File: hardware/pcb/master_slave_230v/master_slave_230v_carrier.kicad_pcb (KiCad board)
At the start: 2 copper layers, 126 x 66 mm, 24 parts, among them J1 AC_IN, J2 5V_SERVICE, J3A MASTER_L, J3B MASTER_R, J4A SLAVE_L, J4B SLAVE_R, J5 PHASE_OUT, J6 MASTER_SIG, J7 SLAVE_SIG, J8 MASTER_DEVKIT_BRIDGE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

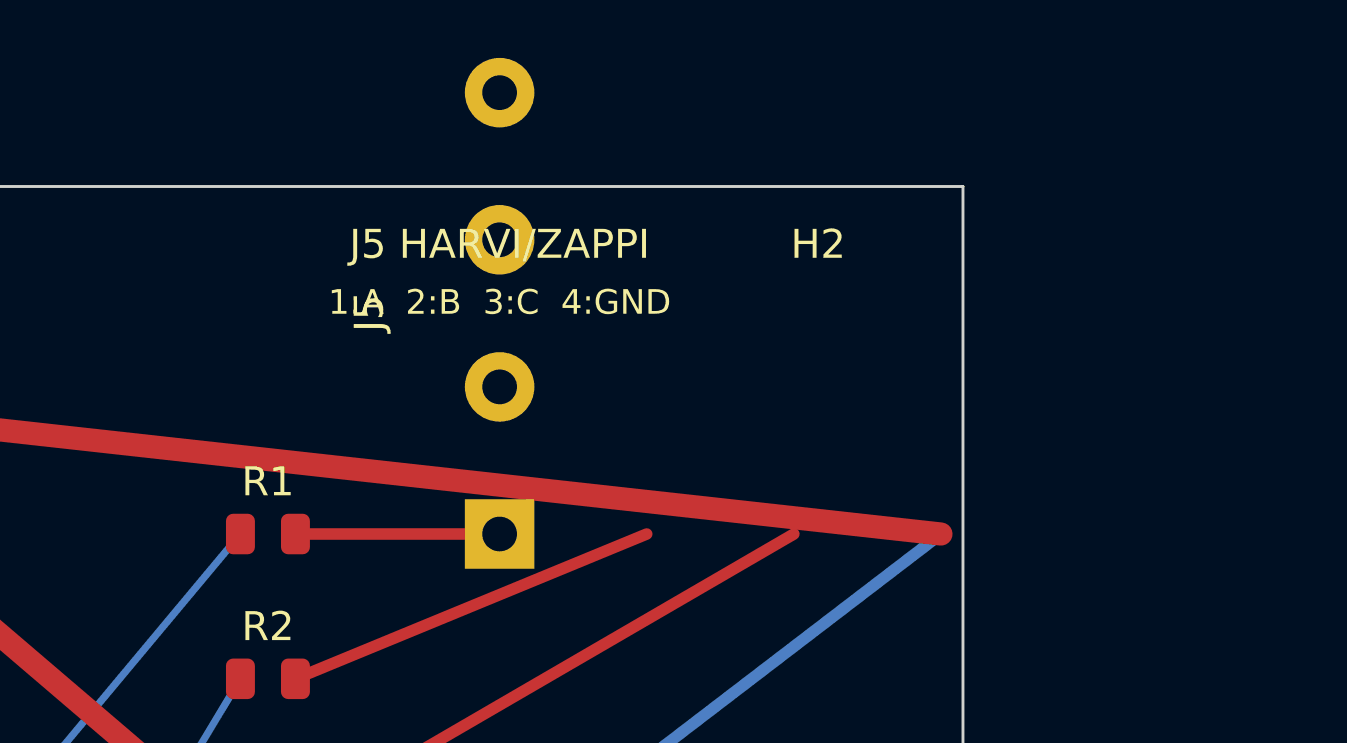
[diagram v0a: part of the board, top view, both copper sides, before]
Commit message: add display
show values/graph
fallback single mode
 -> Phase A = Sum
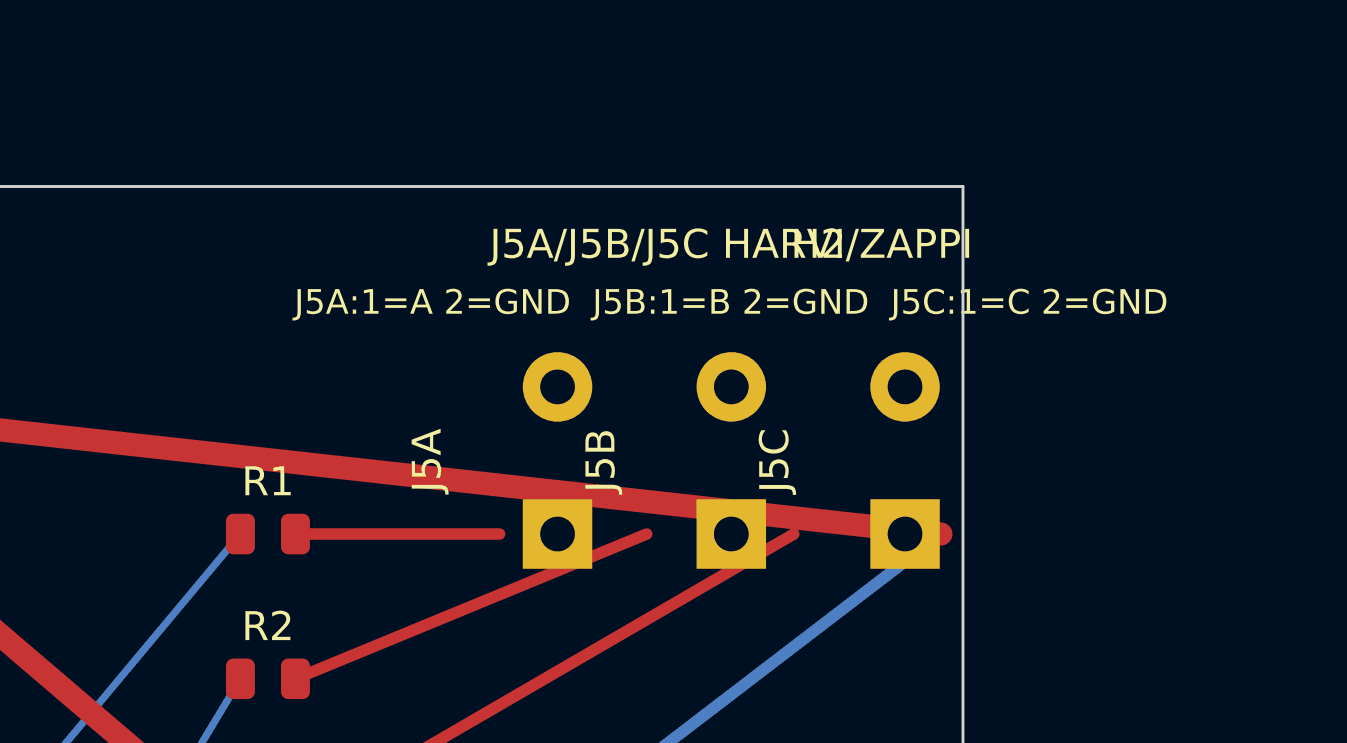
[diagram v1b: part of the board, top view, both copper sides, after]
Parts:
- removed J5: PHASE_OUT, TerminalBlock_Phoenix:TerminalBlock_Phoenix_MKDS-1,5-4_5.08mm
- added J5A: PHASE_A_OUT, TerminalBlock_Phoenix:TerminalBlock_Phoenix_MKDS-1,5-2_5.08mm, F.Cu at (112.0, 12.0)
- added J5B: PHASE_B_OUT, TerminalBlock_Phoenix:TerminalBlock_Phoenix_MKDS-1,5-2_5.08mm, F.Cu at (118.0, 12.0)
- added J5C: PHASE_C_OUT, TerminalBlock_Phoenix:TerminalBlock_Phoenix_MKDS-1,5-2_5.08mm, F.Cu at (124.0, 12.0)
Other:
- board text added: "J5A/J5B/J5C HARVI/ZAPPI"
- board text added: "J5A:1=A 2=GND J5B:1=B 2=GND J5C:1=C 2=GND"
- board text removed: "1:A 2:B 3:C 4:GND"
- board text removed: "J5 HARVI/ZAPPI"
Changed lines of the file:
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@@
   (gr_text "1:+5V  2:GND" (at 84 4 0) (layer "F.SilkS")
     (effects (font (size 0.85 0.85) (thickness 0.12))))
-  (gr_text "J5 HARVI/ZAPPI" (at 110 2 0) (layer "F.SilkS")
+  (gr_text "J5A/J5B/J5C HARVI/ZAPPI" (at 118 2 0) (layer "F.SilkS")
     (effects (font (size 1 1) (thickness 0.15))))
-  (gr_text "1:A  2:B  3:C  4:GND" (at 110 4 0) (layer "F.SilkS")
+  (gr_text "J5A:1=A 2=GND  J5B:1=B 2=GND  J5C:1=C 2=GND" (at 118 4 0) (layer "F.SilkS")
     (effects (font (size 0.85 0.85) (thickness 0.12))))
   (gr_text "HV ZONE" (at 22 33 90) (layer "F.SilkS")
@@
     (pad "2" thru_hole circle (at 5.08 0 90) (size 2.4 2.4) (drill 1.2) (layers "*.Cu" "*.Mask") (net 7 "GND_ISO"))
   )
-  (footprint "TerminalBlock_Phoenix:TerminalBlock_Phoenix_MKDS-1,5-4_5.08mm" (layer "F.Cu")
-    (at 110 12 90)
-    (property "Reference" "J5" (at 7.62 -4.5 90) (layer "F.SilkS")
+  (footprint "TerminalBlock_Phoenix:TerminalBlock_Phoenix_MKDS-1,5-2_5.08mm" (layer "F.Cu")
+    (at 112 12 90)
+    (property "Reference" "J5A" (at 2.54 -4.5 90) (layer "F.SilkS")
       (effects (font (size 1 1) (thickness 0.15))))
-    (property "Value" "PHASE_OUT" (at 7.62 4.5 90) (layer "F.Fab")
+    (property "Value" "PHASE_A_OUT" (at 2.54 4.5 90) (layer "F.Fab")
       (effects (font (size 1 1) (thickness 0.15))))
     (pad "1" thru_hole rect (at 0 0 90) (size 2.4 2.4) (drill 1.2) (layers "*.Cu" "*.Mask") (net 10 "PHASE_A_OUT"))
-    (pad "2" thru_hole circle (at 5.08 0 90) (size 2.4 2.4) (drill 1.2) (layers "*.Cu" "*.Mask") (net 11 "PHASE_B_OUT"))
-    (pad "3" thru_hole circle (at 10.16 0 90) (size 2.4 2.4) (drill 1.2) (layers "*.Cu" "*.Mask") (net 12 "PHASE_C_OUT"))
-    (pad "4" thru_hole circle (at 15.24 0 90) (size 2.4 2.4) (drill 1.2) (layers "*.Cu" "*.Mask") (net 7 "GND_ISO"))
+    (pad "2" thru_hole circle (at 5.08 0 90) (size 2.4 2.4) (drill 1.2) (layers "*.Cu" "*.Mask") (net 7 "GND_ISO"))
+  )
+  (footprint "TerminalBlock_Phoenix:TerminalBlock_Phoenix_MKDS-1,5-2_5.08mm" (layer "F.Cu")
+    (at 118 12 90)
+    (property "Reference" "J5B" (at 2.54 -4.5 90) (layer "F.SilkS")
+      (effects (font (size 1 1) (thickness 0.15))))
+    (property "Value" "PHASE_B_OUT" (at 2.54 4.5 90) (layer "F.Fab")
+      (effects (font (size 1 1) (thickness 0.15))))
+    (pad "1" thru_hole rect (at 0 0 90) (size 2.4 2.4) (drill 1.2) (layers "*.Cu" "*.Mask") (net 11 "PHASE_B_OUT"))
+    (pad "2" thru_hole circle (at 5.08 0 90) (size 2.4 2.4) (drill 1.2) (layers "*.Cu" "*.Mask") (net 7 "GND_ISO"))
+  )
+  (footprint "TerminalBlock_Phoenix:TerminalBlock_Phoenix_MKDS-1,5-2_5.08mm" (layer "F.Cu")
+    (at 124 12 90)
+    (property "Reference" "J5C" (at 2.54 -4.5 90) (layer "F.SilkS")
+      (effects (font (size 1 1) (thickness 0.15))))
+    (property "Value" "PHASE_C_OUT" (at 2.54 4.5 90) (layer "F.Fab")
+      (effects (font (size 1 1) (thickness 0.15))))
+    (pad "1" thru_hole rect (at 0 0 90) (size 2.4 2.4) (drill 1.2) (layers "*.Cu" "*.Mask") (net 12 "PHASE_C_OUT"))
+    (pad "2" thru_hole circle (at 5.08 0 90) (size 2.4 2.4) (drill 1.2) (layers "*.Cu" "*.Mask") (net 7 "GND_ISO"))
   )
   (footprint "Fuse:Fuseholder_5x20mm" (layer "F.Cu")
